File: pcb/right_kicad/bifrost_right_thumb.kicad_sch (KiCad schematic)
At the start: 4 parts, among them SW44 UNASSIGNED_44, SW45 UNASSIGNED_45

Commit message: Use Old Norse Bifrǫst spelling
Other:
- title: Bifröst -> Bifrǫst
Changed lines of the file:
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@@
 	(paper "A3")
 	(title_block
-		(title "Bifröst")
+		(title "Bifrǫst")
 		(company "Hringbord")
 		(comment 1 "Generated by Smiðr KiCad MVP export")

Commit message: Update PCB designs
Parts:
- added C1, C2: 100n, Capacitor_SMD:C_0402_1005Metric, symbol Device:C_Small
- added D1, D2: WS2812B-2020, LED_SMD:LED_WS2812B-2020_PLCC4_2.0x2.0mm, symbol LED:WS2812B-2020
- added J1: Conn_01x05, Connector_PinHeader_1.27mm:PinHeader_1x05_P1.27mm_Vertical, symbol Connector_Generic:Conn_01x05
- SW1: renamed from SW44; value UNASSIGNED_44 -> 1U
- SW2: renamed from SW45; value UNASSIGNED_45 -> 1U
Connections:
- net GND: now also C1.2, C2.2, D1.2 (VSS), D2.2 (VSS), J1.3 (Pin_3)
- net PIN_T2: now reaches SW2.1
- net PIN_T2: now also J1.5 (Pin_5)
- net PIN_T1: now reaches SW1.1
- net PIN_T1: now also J1.4 (Pin_4)
- new net: D1.1 (DOUT), D2.3 (DIN)
- new net RGB: D1.3 (DIN), J1.2 (Pin_2)
- new net RGB_PWR: C1.1, C2.1, D1.4 (VDD), D2.4 (VDD), J1.1 (Pin_1)
- no-connect marks 0 -> 1
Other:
- moved on the sheet: H1, H2

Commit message: Update Bifrost case and PCB outputs
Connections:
- net GND: now also J1.2 (Pin_2); no longer J1.3 (Pin_3)
- net RGB: now also J1.3 (Pin_3); no longer J1.2 (Pin_2)
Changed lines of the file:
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@@
 	(global_label "RGB"
 		(shape output)
-		(at 127 129.54 180)
+		(at 127 132.08 180)
 		(fields_autoplaced yes)
 		(effects
@@
 		)
 		(property "Intersheetrefs" "${INTERSHEET_REFS}"
-			(at 120.2048 129.54 0)
+			(at 120.2048 132.08 0)
 			(hide yes)
 			(show_name no)
@@
 	(symbol
 		(lib_id "power:GND")
-		(at 127 132.08 270)
+		(at 127 129.54 270)
 		(unit 1)
 		(body_style 1)
@@
 		(fields_autoplaced yes)
 		(property "Reference" "#PWR01"
-			(at 120.65 132.08 0)
+			(at 120.65 129.54 0)
 			(hide yes)
 			(show_name no)
@@
 		)
 		(property "Value" "GND"
-			(at 123.19 132.0799 90)
+			(at 123.19 129.5399 90)
 			(show_name no)
 			(do_not_autoplace no)
@@
 		)
 		(property "Footprint" ""
-			(at 127 132.08 0)
-			(hide yes)
-			(show_name no)
-			(do_not_autoplace no)
-			(effects
-				(font
-					(size 1.27 1.27)
-				)
-			)
-		)
-		(property "Datasheet" ""
-			(at 127 132.08 0)
+			(at 127 129.54 0)
+			(hide yes)
+			(show_name no)
+			(do_not_autoplace no)
+			(effects
+				(font
+					(size 1.27 1.27)
+				)
+			)
+		)
+		(property "Datasheet" ""
+			(at 127 129.54 0)
 			(hide yes)
 			(show_name no)
@@
 		)
 		(property "Description" ""
-			(at 127 132.08 0)
-			(show_name no)
-			(do_not_autoplace no)
+			(at 127 129.54 0)
+			(show_name no)
+			(do_not_autoplace no)

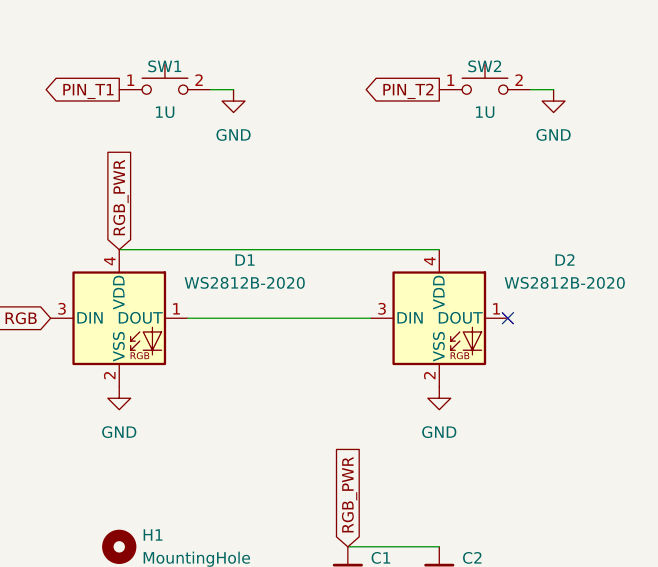
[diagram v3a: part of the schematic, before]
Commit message: Update PCB designs and production files
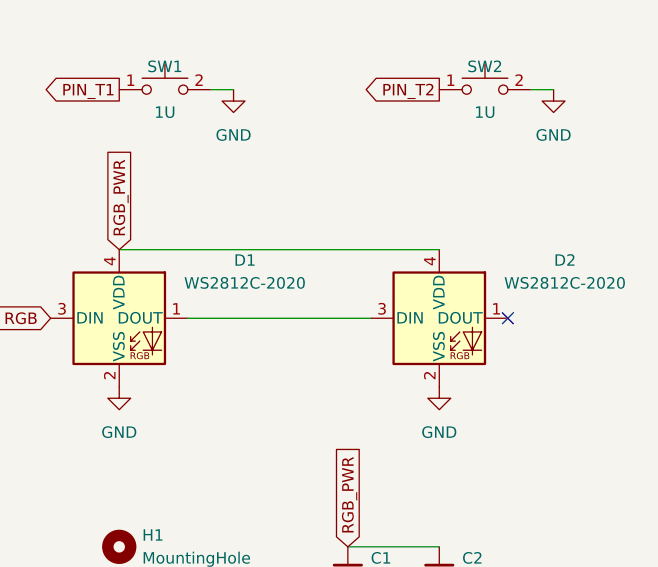
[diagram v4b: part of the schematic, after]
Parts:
- C1, C2: JLCPCB Part # (none) -> C1525
- D1, D2: value WS2812B-2020 -> WS2812C-2020; JLCPCB Part # (none) -> C55109522
- J1: now left out of the parts list
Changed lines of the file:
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@@
 		(body_style 1)
 		(exclude_from_sim no)
-		(in_bom yes)
-		(on_board yes)
-		(in_pos_files yes)
+		(in_bom no)
+		(on_board yes)
+		(in_pos_files no)
 		(dnp no)
 		(fields_autoplaced yes)
@@
 			)
 		)
-		(property "Value" "WS2812B-2020"
+		(property "Value" "WS2812C-2020"
 			(at 140.97 173.9198 0)
 			(show_name no)
@@
 		)
 		(property "Description" "RGB LED with integrated controller, 2.0 x 2.0 mm, 12 mA"
+			(at 127 177.8 0)
+			(hide yes)
+			(show_name no)
+			(do_not_autoplace no)
+			(effects
+				(font
+					(size 1.27 1.27)
+				)
+			)
+		)
+		(property "JLCPCB Part #" "C55109522"
 			(at 127 177.8 0)
 			(hide yes)
@@
 			)
 		)
+		(property "JLCPCB Part #" "C1525 "
+			(at 152.4 205.74 0)
+			(hide yes)
+			(show_name no)
+			(do_not_autoplace no)
+			(effects
+				(font
+					(size 1.27 1.27)
+				)
+			)
+		)
 		(pin "1"
 		)
@@
 			)
 		)
+		(property "JLCPCB Part #" "C1525 "
+			(at 162.56 205.74 0)
+			(hide yes)
+			(show_name no)
+			(do_not_autoplace no)
+			(effects
+				(font
+					(size 1.27 1.27)
+				)
+			)
+		)
 		(pin "1"
 		)
@@
 			)
 		)
-		(property "Value" "WS2812B-2020"
+		(property "Value" "WS2812C-2020"
 			(at 176.53 173.9198 0)
 			(show_name no)
@@
 			(at 162.56 177.8 0)
 			(hide yes)
+			(show_name no)
+			(do_not_autoplace no)
+			(effects
+				(font
+					(size 1.27 1.27)
+				)
+			)
+		)
+		(property "JLCPCB Part #" "C55109522"
+			(at 162.56 177.8 0)
+			(hide yes)

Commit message: Update PCB mounting hardware footprints
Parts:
- H1, H2: footprint Smidr:MountingHole_TH-1.6-M2 -> Smidr:SMD-1_BD4.4-D2.8; JLCPCB Part # C2928170 -> C2928179
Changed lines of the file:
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@@
 			)
 		)
-		(property "Footprint" "Smidr:MountingHole_TH-1.6-M2"
+		(property "Footprint" "Smidr:SMD-1_BD4.4-D2.8"
 			(at 127 203.2 0)
 			(hide yes)
@@
 			)
 		)
-		(property "JLCPCB Part #" "C2928170"
+		(property "JLCPCB Part #" "C2928179"
 			(at 127 203.2 0)
 			(hide yes)
@@
 			)
 		)
-		(property "Footprint" "Smidr:MountingHole_TH-1.6-M2"
+		(property "Footprint" "Smidr:SMD-1_BD4.4-D2.8"
 			(at 127 208.28 0)
 			(hide yes)
@@
 			)
 		)
-		(property "JLCPCB Part #" "C2928170"
+		(property "JLCPCB Part #" "C2928179"
 			(at 127 208.28 0)
 			(hide yes)
